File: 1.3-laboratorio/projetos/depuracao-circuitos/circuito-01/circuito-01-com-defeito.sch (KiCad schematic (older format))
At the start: 22 parts, among them J1 Conn_01x07_Male, J2 Conn_01x07_Male, J3 Conn_01x07_Male, J4 Conn_01x07_Male, J5 Conn_01x07_Male, J6 Conn_01x07_Male, J7 Conn_01x05, J8 Conn_01x05, P1 CONN_01X02, SW1 SW_DIP_x04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

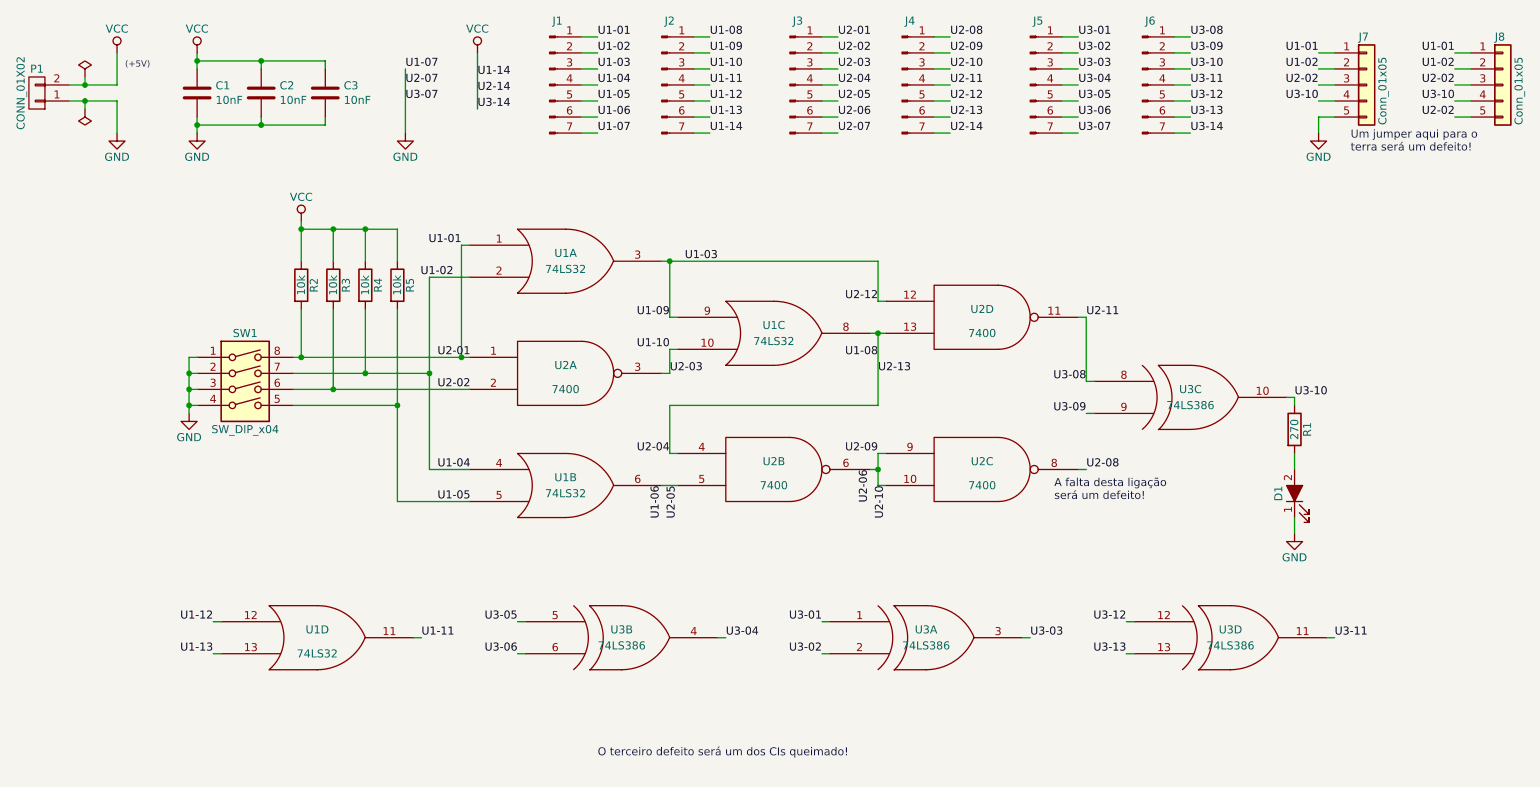
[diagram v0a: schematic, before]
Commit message: Troca do 74LS386 pelo 74LS86 e correspondentes ajustes no esquemático e na PCI.
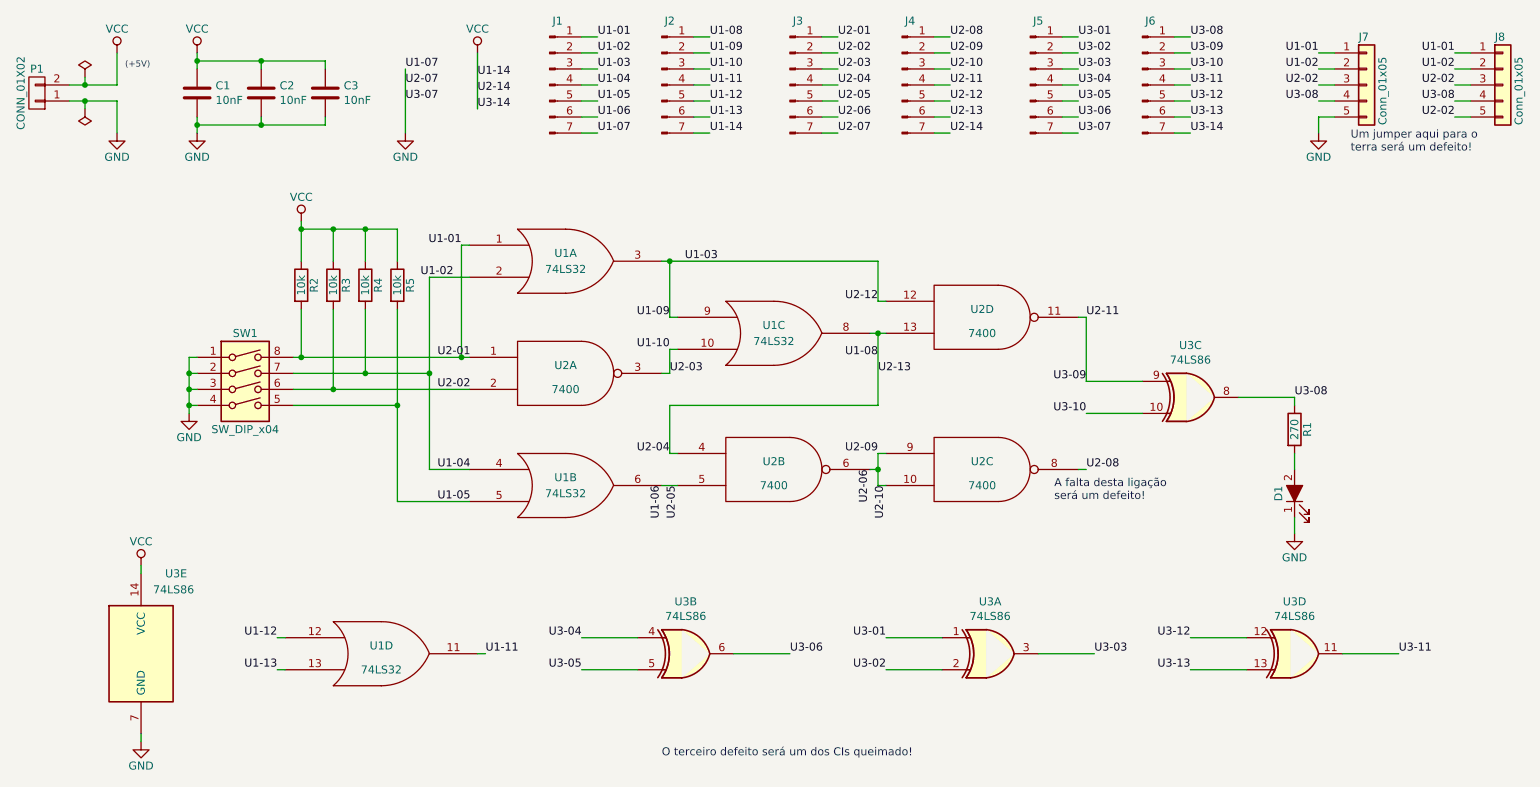
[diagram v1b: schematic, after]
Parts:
- removed U3: 74LS386, Package_DIP:DIP-14_W7.62mm_Socket_LongPads, symbol circuito-01-rescue:74LS386
- added U3: 74LS86, Package_DIP:DIP-14_W7.62mm_Socket_LongPads, symbol 74xx:74LS86
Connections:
- net U3-09 is gone; now on net U2-11: J6.2 (Pin_2)
- net GND: now also U3.7 (GND)
- net U2-11: now also U3.9; no longer J6.1 (Pin_1)
- net U3-01: now also U3.1
- net U3-02: now also U3.2
- net U3-03: now also U3.3
- net U3-04: now also U3.4
- net U3-05: now also U3.5
- net U3-06: now also U3.6
- net U3-10: now also U3.10; no longer J7.4 (Pin_4), J8.4 (Pin_4), R1.1
- net U3-11: now also U3.11
- net U3-12: now also U3.12
- net U3-13: now also U3.13
- net VCC: now also U3.14 (VCC)
- new net U3-08: J6.1 (Pin_1), J7.4 (Pin_4), J8.4 (Pin_4), R1.1, U3.8
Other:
- moved on the sheet: U1D
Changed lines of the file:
@@
 EESchema Schematic File Version 4
+LIBS:circuito-01-com-defeito-cache
 EELAYER 26 0
 EELAYER END
@@
 Sheet 1 1
 Title "Depuração de Circuitos - Circuito 01"
-Date "2019-04-21"
-Rev "02"
+Date "2019-11-14"
+Rev "03"
 Comp "ETE102 - Fundamentos de Circuitos Digitais"
 Comment1 "Licença: CC-BY-SA (http://creativecommons.org/licenses/by-sa/4.0/)"
@@
 $EndComp
 $Comp
-L circuito-01-rescue:74LS386 U3
-U 3 1 5B0DB8C7
-P 8500 3850
-F 0 "U3" H 8500 3900 50  0000 C CNN
-F 1 "74LS386" H 8500 3800 50  0000 C CNN
-F 2 "Package_DIP:DIP-14_W7.62mm_Socket_LongPads" H 8500 3850 50  0001 C CNN
-F 3 "" H 8500 3850 50  0001 C CNN
-	3    8500 3850
-	1    0    0    -1
-$EndComp
-$Comp
 L circuito-01-rescue:R R1
 U 1 1 5B0DF334
@@
 Connection ~ 6550 4300
 Wire Wire Line
-	7900 3750 7850 3750
-Wire Wire Line
 	7850 3750 7850 3350
 Wire Wire Line
 	7850 3350 7800 3350
 Wire Wire Line
-	7900 3950 7850 3950
-Wire Wire Line
 	9150 3850 9150 3900
 Wire Wire Line
-	9150 3850 9100 3850
+	9150 3850 8800 3850
 Wire Wire Line
 	6600 4200 6550 4200
@@
 U2-08
 Text Label 7850 3950 2    50   ~ 0
+U3-10
+Text Label 7850 3750 2    50   ~ 0
 U3-09
-Text Label 7850 3750 2    50   ~ 0
+Text Label 9150 3850 0    50   ~ 0
 U3-08
-Text Label 9150 3850 0    50   ~ 0
-U3-10
 $Comp
 L circuito-01-rescue:GND #PWR0101
@@
 L circuito-01-rescue:74LS32 U1
 U 4 1 5CCB6625
-P 3050 5350
-F 0 "U1" H 3050 5400 50  0000 C CNN
-F 1 "74LS32" H 3050 5250 50  0000 C CNN
-F 2 "Package_DIP:DIP-14_W7.62mm_Socket_LongPads" H 3050 5350 50  0001 C CNN
-F 3 "" H 3050 5350 50  0001 C CNN
-	4    3050 5350
-	1    0    0    -1
-$EndComp
-$Comp
-L circuito-01-rescue:74LS386 U3
-U 2 1 5CCB66E7
-P 4950 5350
-F 0 "U3" H 4950 5400 50  0000 C CNN
-F 1 "74LS386" H 4950 5300 50  0000 C CNN
-F 2 "Package_DIP:DIP-14_W7.62mm_Socket_LongPads" H 4950 5350 50  0001 C CNN
-F 3 "" H 4950 5350 50  0001 C CNN
-	2    4950 5350
-	1    0    0    -1
-$EndComp
-$Comp
-L circuito-01-rescue:74LS386 U3
-U 1 1 5CCB67AB
-P 6850 5350
-F 0 "U3" H 6850 5400 50  0000 C CNN
-F 1 "74LS386" H 6850 5300 50  0000 C CNN
-F 2 "Package_DIP:DIP-14_W7.62mm_Socket_LongPads" H 6850 5350 50  0001 C CNN
-F 3 "" H 6850 5350 50  0001 C CNN
-	1    6850 5350
-	1    0    0    -1
-$EndComp
-$Comp
-L circuito-01-rescue:74LS386 U3
-U 4 1 5CCB6825
-P 8750 5350
-F 0 "U3" H 8750 5400 50  0000 C CNN
-F 1 "74LS386" H 8750 5300 50  0000 C CNN
-F 2 "Package_DIP:DIP-14_W7.62mm_Socket_LongPads" H 8750 5350 50  0001 C CNN
-F 3 "" H 8750 5350 50  0001 C CNN
-	4    8750 5350
-	1    0    0    -1
-$EndComp
-Wire Wire Line
-	2450 5250 2400 5250
-Wire Wire Line
-	2450 5450 2400 5450
-Wire Wire Line
-	3650 5350 3700 5350
-Wire Wire Line
-	4350 5250 4300 5250
-Wire Wire Line
-	4350 5450 4300 5450
-Wire Wire Line
-	5550 5350 5600 5350
-Wire Wire Line
-	6250 5250 6200 5250
-Wire Wire Line
-	6250 5450 6200 5450
-Wire Wire Line
-	7450 5350 7500 5350
-Wire Wire Line
-	8150 5250 8100 5250
-Wire Wire Line
-	8150 5450 8100 5450
-Wire Wire Line
-	9350 5350 9400 5350
-Text Label 2400 5250 2    50   ~ 0
+P 3450 5450
+F 0 "U1" H 3450 5500 50  0000 C CNN
+F 1 "74LS32" H 3450 5350 50  0000 C CNN
+F 2 "Package_DIP:DIP-14_W7.62mm_Socket_LongPads" H 3450 5450 50  0001 C CNN
+F 3 "" H 3450 5450 50  0001 C CNN
+	4    3450 5450
+	1    0    0    -1
+$EndComp
+Wire Wire Line
+	2850 5350 2800 5350
+Wire Wire Line
+	2850 5550 2800 5550
+Wire Wire Line
+	4050 5450 4100 5450
+Text Label 2800 5350 2    50   ~ 0
 U1-12
-Text Label 2400 5450 2    50   ~ 0
+Text Label 2800 5550 2    50   ~ 0
 U1-13
-Text Label 3700 5350 0    50   ~ 0
+Text Label 4100 5450 0    50   ~ 0
 U1-11
-Text Label 4300 5250 2    50   ~ 0
+Text Label 4700 5350 2    50   ~ 0
+U3-04
+Text Label 4700 5550 2    50   ~ 0
 U3-05
-Text Label 4300 5450 2    50   ~ 0
+Text Label 6600 5350 2    50   ~ 0
+U3-01
+Text Label 6600 5550 2    50   ~ 0
+U3-02
+Text Label 8500 5350 2    50   ~ 0
+U3-12
+Text Label 8500 5550 2    50   ~ 0
+U3-13
+Text Label 9800 5450 0    50   ~ 0
+U3-11
+Text Label 7900 5450 0    50   ~ 0
+U3-03
+Text Label 6000 5450 0    50   ~ 0
 U3-06
-Text Label 6200 5250 2    50   ~ 0
-U3-01
-Text Label 6200 5450 2    50   ~ 0
-U3-02
-Text Label 8100 5250 2    50   ~ 0
-U3-12
-Text Label 8100 5450 2    50   ~ 0
-U3-13
-Text Label 9400 5350 0    50   ~ 0
-U3-11
-Text Label 7500 5350 0    50   ~ 0
-U3-03
-Text Label 5600 5350 0    50   ~ 0
-U3-04
 $Comp
 L circuito-01-rescue:VCC #PWR0103
@@
 U2-02
 Text Label 9300 2000 2    50   ~ 0
-U3-10
+U3-08
 Text Label 10150 2000 2    50   ~ 0
-U3-10
+U3-08
 Text Label 9300 1800 2    50   ~ 0
 U1-02
@@
 Text Notes 7650 4500 0    50   ~ 0
 A falta desta ligação\nserá um defeito!
-Text Notes 4800 6100 0    50   ~ 0
+Text Notes 5200 6100 0    50   ~ 0
 O terceiro defeito será um dos CIs queimado!
 Wire Wire Line
@@
 Text Label 10150 2100 2    50   ~ 0
 U2-02
+$Comp
+L 74xx:74LS86 U3
+U 3 1 5DCDE195
+P 8500 3850
+F 0 "U3" H 8500 4175 50  0000 C CNN
+F 1 "74LS86" H 8500 4084 50  0000 C CNN
+F 2 "Package_DIP:DIP-14_W7.62mm_Socket_LongPads" H 8500 3850 50  0001 C CNN
+F 3 "74xx/74ls86.pdf" H 8500 3850 50  0001 C CNN
+	3    8500 3850
+	1    0    0    -1
+$EndComp
+Wire Wire Line
+	7850 3750 8200 3750
+Wire Wire Line
+	7850 3950 8200 3950
+$Comp
+L 74xx:74LS86 U3
+U 2 1 5DCF3D68
+P 5350 5450
+F 0 "U3" H 5350 5775 50  0000 C CNN
+F 1 "74LS86" H 5350 5684 50  0000 C CNN
+F 2 "Package_DIP:DIP-14_W7.62mm_Socket_LongPads" H 5350 5450 50  0001 C CNN
+F 3 "74xx/74ls86.pdf" H 5350 5450 50  0001 C CNN
+	2    5350 5450
+	1    0    0    -1
+$EndComp
+$Comp
+L 74xx:74LS86 U3
+U 1 1 5DCF3E4E
+P 7250 5450
+F 0 "U3" H 7250 5775 50  0000 C CNN
+F 1 "74LS86" H 7250 5684 50  0000 C CNN
+F 2 "Package_DIP:DIP-14_W7.62mm_Socket_LongPads" H 7250 5450 50  0001 C CNN
+F 3 "74xx/74ls86.pdf" H 7250 5450 50  0001 C CNN
+	1    7250 5450
+	1    0    0    -1
+$EndComp
+$Comp
+L 74xx:74LS86 U3
+U 4 1 5DCF3F0C
+P 9150 5450
+F 0 "U3" H 9150 5775 50  0000 C CNN
+F 1 "74LS86" H 9150 5684 50  0000 C CNN
+F 2 "Package_DIP:DIP-14_W7.62mm_Socket_LongPads" H 9150 5450 50  0001 C CNN
+F 3 "74xx/74ls86.pdf" H 9150 5450 50  0001 C CNN
+	4    9150 5450
+	1    0    0    -1
+$EndComp
+Wire Wire Line
+	4700 5350 5050 5350
+Wire Wire Line
+	4700 5550 5050 5550
+Wire Wire Line
+	5650 5450 6000 5450
+Wire Wire Line
+	6600 5350 6950 5350
+Wire Wire Line
+	6600 5550 6950 5550
+Wire Wire Line
+	7550 5450 7900 5450
+Wire Wire Line
+	8500 5350 8850 5350
+Wire Wire Line
+	8500 5550 8850 5550
+Wire Wire Line
+	9450 5450 9800 5450
+$Comp
+L 74xx:74LS86 U3
+U 5 1 5DCE53BD
+P 1950 5450
+F 0 "U3" H 2100 5950 50  0000 L CNN
+F 1 "74LS86" H 2025 5850 50  0000 L CNN
+F 2 "Package_DIP:DIP-14_W7.62mm_Socket_LongPads" H 1950 5450 50  0001 C CNN
+F 3 "74xx/74ls86.pdf" H 1950 5450 50  0001 C CNN
+	5    1950 5450
+	1    0    0    -1
+$EndComp
+$Comp
+L circuito-01-rescue:VCC #PWR?
+U 1 1 5DCE5C59
+P 1950 4900
+F 0 "#PWR?" H 1950 4750 50  0001 C CNN
+F 1 "VCC" H 1950 5050 50  0000 C CNN
+F 2 "" H 1950 4900 50  0000 C CNN
+F 3 "" H 1950 4900 50  0000 C CNN
+	1    1950 4900
+	1    0    0    -1
+$EndComp
+$Comp
+L circuito-01-rescue:GND #PWR?
+U 1 1 5DCE5CA4
+P 1950 6000
+F 0 "#PWR?" H 1950 5750 50  0001 C CNN
+F 1 "GND" H 1950 5850 50  0000 C CNN
+F 2 "" H 1950 6000 50  0000 C CNN
+F 3 "" H 1950 6000 50  0000 C CNN
+	1    1950 6000
+	1    0    0    -1
+$EndComp
+Wire Wire Line
+	1950 5950 1950 6000
+Wire Wire Line
+	1950 4950 1950 4900
 $EndSCHEMATC

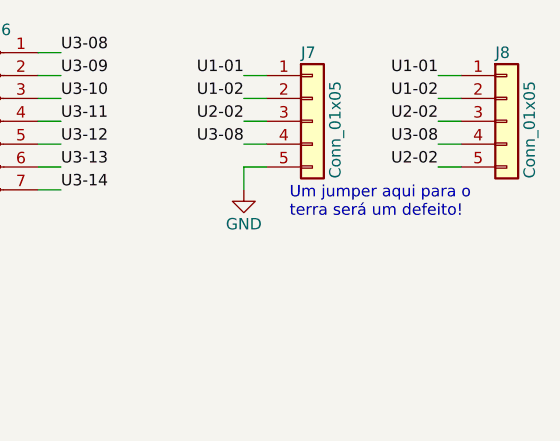
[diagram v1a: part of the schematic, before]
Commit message: Alteração de trilha para provocar curto intencional na variável 'B' ao invés da 'C', pois esta não influencia na saída.
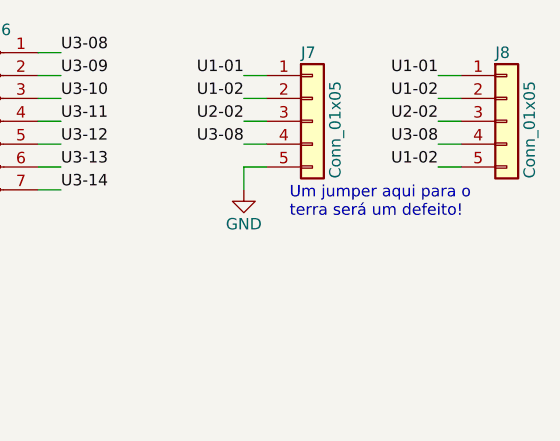
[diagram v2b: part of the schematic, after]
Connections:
- net U1-02: now also J8.5 (Pin_5)
- net U2-02: no longer J8.5 (Pin_5)
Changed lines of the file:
@@
 Sheet 1 1
 Title "Depuração de Circuitos - Circuito 01"
-Date "2019-11-14"
-Rev "03"
+Date "2019-11-24"
+Rev "04"
 Comp "ETE102 - Fundamentos de Circuitos Digitais"
 Comment1 "Licença: CC-BY-SA (http://creativecommons.org/licenses/by-sa/4.0/)"
@@
 	10150 2100 10250 2100
 Text Label 10150 2100 2    50   ~ 0
-U2-02
+U1-02
 $Comp
 L 74xx:74LS86 U3
@@
 $EndComp
 $Comp
-L circuito-01-rescue:VCC #PWR?
+L circuito-01-rescue:VCC #PWR0106
 U 1 1 5DCE5C59
 P 1950 4900
-F 0 "#PWR?" H 1950 4750 50  0001 C CNN
+F 0 "#PWR0106" H 1950 4750 50  0001 C CNN
 F 1 "VCC" H 1950 5050 50  0000 C CNN
 F 2 "" H 1950 4900 50  0000 C CNN
@@
 $EndComp
 $Comp
-L circuito-01-rescue:GND #PWR?
+L circuito-01-rescue:GND #PWR0107
 U 1 1 5DCE5CA4
 P 1950 6000
-F 0 "#PWR?" H 1950 5750 50  0001 C CNN
+F 0 "#PWR0107" H 1950 5750 50  0001 C CNN
 F 1 "GND" H 1950 5850 50  0000 C CNN
 F 2 "" H 1950 6000 50  0000 C CNN
